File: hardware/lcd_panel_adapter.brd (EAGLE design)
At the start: 54 x 30 mm, 50 parts, among them IC1 TPS65131RGET, IC2 LP8867CQPWPRQ1, J1 245863050104829+, J2 54548-2271, U1 TLV62080DSGR

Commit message: added +1.8V pullup resistor for LCD reset pin
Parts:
- added R16: 10k, rcl:R0603
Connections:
- net 1V8: now also R16.2
- net LCD_RESET_N: now also R16.1
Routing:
- net LCD_RESET_N: track 24.2 -> 43.9 mm
- net 1V8: track 33.3 -> 35.9 mm
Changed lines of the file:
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@@
 </element>
 <element name="R7" library="rcl" library_urn="urn:adsk.eagle:library:334" package="R0603" package3d_urn="urn:adsk.eagle:package:23555/3" value="150k" x="12" y="22.5" smashed="yes" rot="R90">
-<attribute name="NAME" x="12.745" y="25.925" size="0.8128" layer="25" rot="R180"/>
+<attribute name="NAME" x="14.095" y="24.875" size="0.8128" layer="25" rot="R180"/>
 <attribute name="POPULARITY" value="70" x="12" y="22.5" size="1.778" layer="27" rot="R90" display="off"/>
 <attribute name="SPICEPREFIX" value="R" x="12" y="22.5" size="1.778" layer="27" rot="R90" display="off"/>
@@
 <attribute name="SPICEPREFIX" value="C" x="35.71" y="26.09" size="1.778" layer="27" rot="R90" display="off"/>
 <attribute name="VALUE" x="38.25" y="24.82" size="1.27" layer="27" rot="R90"/>
+</element>
+<element name="R16" library="rcl" library_urn="urn:adsk.eagle:library:334" package="R0603" package3d_urn="urn:adsk.eagle:package:23555/3" value="10k" x="12.55" y="26.6" smashed="yes" rot="R270">
+<attribute name="NAME" x="11.165" y="25.615" size="0.8128" layer="25" rot="R90"/>
+<attribute name="POPULARITY" value="70" x="12.55" y="26.6" size="1.778" layer="27" rot="R270" display="off"/>
+<attribute name="SPICEPREFIX" value="R" x="12.55" y="26.6" size="1.778" layer="27" rot="R270" display="off"/>
+<attribute name="VALUE" x="10.645" y="27.235" size="1.27" layer="27" rot="R270"/>
 </element>
 </elements>
@@
 <wire x1="26.94" y1="23.96" x2="27.596" y2="24.616" width="0.127" layer="1"/>
 <wire x1="27.596" y1="24.616" x2="27.6" y2="24.616" width="0.127" layer="1"/>
+<wire x1="45.648" y1="17.375" x2="51.51" y2="19.41" width="0" layer="19" extent="1-1"/>
+<wire x1="42.71" y1="15.39" x2="42.71" y2="16.4" width="0" layer="19" extent="1-1"/>
+<wire x1="45.648" y1="14.775" x2="45.648" y2="17.375" width="0" layer="19" extent="1-1"/>
+<wire x1="39.772" y1="14.125" x2="42.66" y2="15.34" width="0" layer="19" extent="1-1"/>
+<wire x1="39.8" y1="10.55" x2="38.33" y2="13.62" width="0" layer="19" extent="1-1"/>
+<wire x1="35.14" y1="16.83" x2="38.33" y2="13.62" width="0" layer="19" extent="1-1"/>
+<wire x1="35" y1="19" x2="35.14" y2="16.83" width="0" layer="19" extent="1-1"/>
+<wire x1="35.29" y1="22.44" x2="35" y2="19" width="0" layer="19" extent="1-1"/>
+<wire x1="37.39" y1="22.45" x2="35.3" y2="22.45" width="0" layer="19" extent="1-1"/>
+<wire x1="39.5" y1="22.45" x2="37.4" y2="22.45" width="0" layer="19" extent="1-1"/>
+<wire x1="32.21" y1="25.395" x2="35.3" y2="22.45" width="0" layer="19" extent="1-1"/>
+<wire x1="35.7" y1="27.5" x2="35.71" y2="27.49" width="0" layer="19" extent="1-1"/>
+<wire x1="38.7" y1="27.5" x2="38.68" y2="27.48" width="0" layer="19" extent="1-1"/>
+<wire x1="16.57" y1="23.81" x2="18.74" y2="23.83" width="0" layer="19" extent="1-1"/>
+<wire x1="12" y1="23.35" x2="15.02" y2="23.81" width="0" layer="19" extent="1-1"/>
+<wire x1="9.86" y1="23.39" x2="12" y2="23.35" width="0" layer="19" extent="1-1"/>
+<wire x1="9.53" y1="18.9" x2="9.86" y2="22.15" width="0" layer="19" extent="1-1"/>
+<wire x1="8.28" y1="16.95" x2="9" y2="17.7" width="0" layer="19" extent="1-1"/>
+<wire x1="6.33" y1="17.7" x2="6.33" y2="17.2" width="0" layer="19" extent="1-1"/>
+<wire x1="9" y1="16.2" x2="8.28" y2="16.95" width="0" layer="19" extent="1-1"/>
+<wire x1="15.19" y1="27.47" x2="15.02" y2="23.81" width="0" layer="19" extent="1-1"/>
+<wire x1="17.26" y1="28.7" x2="15.19" y2="28.68" width="0" layer="19" extent="1-1"/>
+<wire x1="13.25" y1="19.9" x2="12" y2="23.35" width="0" layer="19" extent="1-1"/>
+<wire x1="14.1" y1="18.15" x2="14.52" y2="19.9" width="0" layer="19" extent="1-1"/>
+<wire x1="17.97" y1="18.8" x2="15.54" y2="18.15" width="0" layer="19" extent="1-1"/>
+<wire x1="20.13" y1="18.76" x2="17.97" y2="18.8" width="0" layer="19" extent="1-1"/>
+<wire x1="2.3" y1="15.15" x2="6.33" y2="17.2" width="0" layer="19" extent="1-1"/>
+<wire x1="2.75" y1="13.4" x2="2.3" y2="15.15" width="0" layer="19" extent="1-1"/>
+<wire x1="4.62" y1="11.12" x2="2.75" y2="13.4" width="0" layer="19" extent="1-1"/>
+<wire x1="8.6" y1="8.55" x2="6.63" y2="11.14" width="0" layer="19" extent="1-1"/>
+<wire x1="5.84" y1="7.94" x2="8.6" y2="8.55" width="0" layer="19" extent="1-1"/>
+<wire x1="7.63" y1="5.19" x2="5.8" y2="6.75" width="0" layer="19" extent="1-1"/>
+<wire x1="25.42" y1="13.06" x2="20.13" y2="17.3" width="0" layer="19" extent="1-1"/>
+<wire x1="25.54" y1="10.43" x2="25.42" y2="13.06" width="0" layer="19" extent="1-1"/>
+<wire x1="26.56" y1="8.81" x2="25.54" y2="10.43" width="0" layer="19" extent="1-1"/>
+<wire x1="26.89" y1="6.33" x2="26.56" y2="8.81" width="0" layer="19" extent="1-1"/>
+<wire x1="25.39" y1="6.33" x2="26.89" y2="6.33" width="0" layer="19" extent="1-1"/>
+<wire x1="22.39" y1="6.33" x2="23.89" y2="6.33" width="0" layer="19" extent="1-1"/>
+<wire x1="17.12" y1="4.43" x2="17.115" y2="4.43" width="0" layer="19" extent="1-1"/>
+<wire x1="32.16" y1="4.43" x2="28.39" y2="6.33" width="0" layer="19" extent="1-1"/>
 </signal>
 <signal name="+5V">
@@
 <wire x1="15.06" y1="11.06" x2="16.3722" y2="12.3722" width="0.4" layer="15"/>
 <wire x1="13.82" y1="22.85" x2="13.82" y2="24.7" width="0.4" layer="15"/>
-<wire x1="13.82" y1="24.7" x2="14.89" y2="25.77" width="0.4" layer="15"/>
+<wire x1="13.82" y1="24.7" x2="14.06" y2="24.94" width="0.4" layer="15"/>
+<wire x1="14.06" y1="24.94" x2="14.89" y2="25.77" width="0.4" layer="15"/>
 <wire x1="14.89" y1="25.77" x2="15.19" y2="25.77" width="0.4" layer="15"/>
 <via x="15.19" y="25.77" extent="1-16" drill="0.35"/>
 <wire x1="13.51" y1="9.51" x2="15.06" y2="11.06" width="0.4" layer="1"/>
 <wire x1="16.3722" y1="20.2978" x2="13.82" y2="22.85" width="0.4" layer="15"/>
+<contactref element="R16" pad="2"/>
+<wire x1="12.55" y1="25.75" x2="12.58" y2="25.78" width="0.4" layer="1"/>
+<wire x1="12.58" y1="25.78" x2="15.2" y2="25.78" width="0.4" layer="1"/>
 </signal>
 <signal name="FB">
@@
 <wire x1="48.9" y1="29.64" x2="51.51" y2="27.03" width="0.127" layer="1"/>
 <wire x1="31.04" y1="29.64" x2="48.9" y2="29.64" width="0.127" layer="1"/>
+<contactref element="R16" pad="1"/>
+<wire x1="12.55" y1="27.45" x2="12.55" y2="27.95" width="0.127" layer="1"/>
+<wire x1="14.24" y1="29.64" x2="31.04" y2="29.64" width="0.127" layer="1"/>
+<wire x1="12.55" y1="27.95" x2="14.24" y2="29.64" width="0.127" layer="1"/>
 </signal>
 <signal name="LCD_BL_LEDPWM">

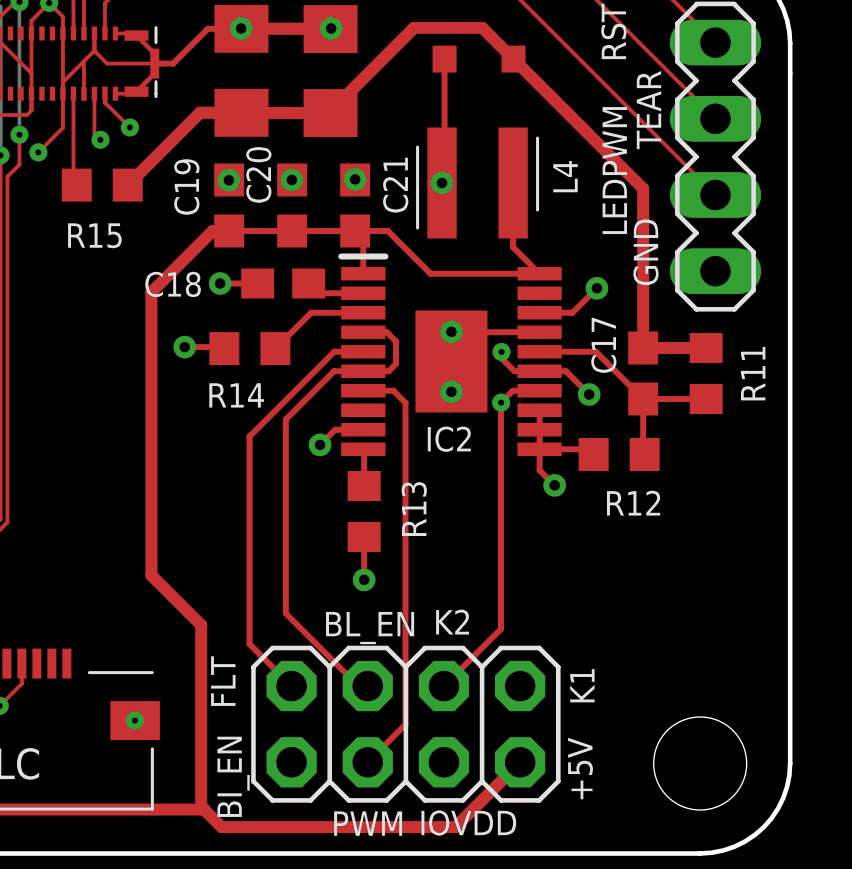
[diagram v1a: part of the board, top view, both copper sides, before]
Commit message: updated the backlight driver IC from LP8867 to TPS61194
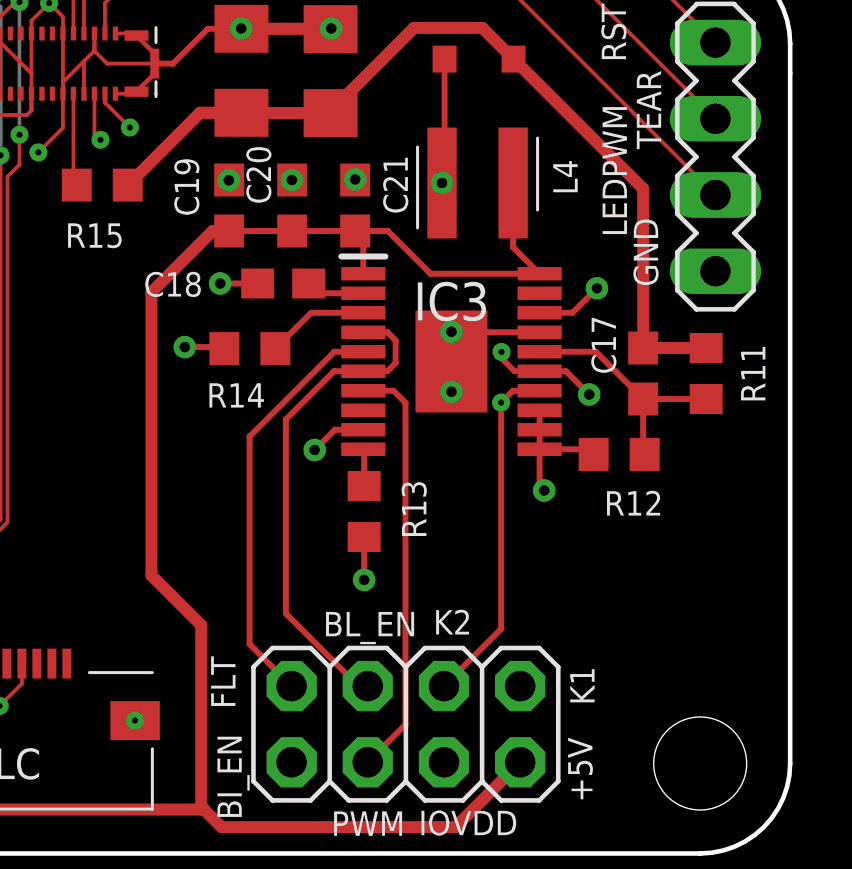
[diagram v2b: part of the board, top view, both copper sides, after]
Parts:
- C12: value 12pF -> 75pF
- C8: value 15pF -> 12pF
- IC3: value LP8867CQPWPRQ1 -> TPS61194PWPR
- R13: value 60k -> 62k
- renumbered IC2 to IC3
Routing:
- net LCD_BL_K2: track 30.8 -> 29.3 mm
- net GND: track 114.5 -> 115.0 mm

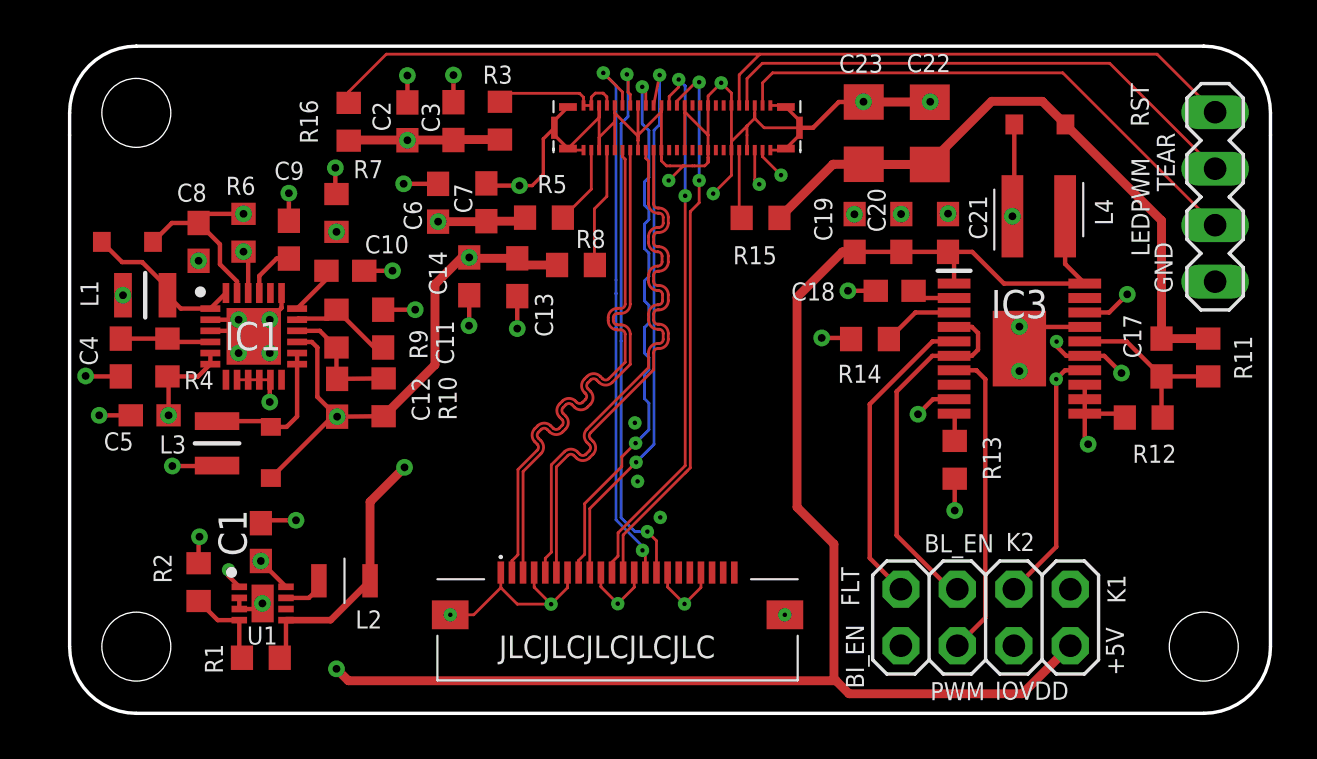
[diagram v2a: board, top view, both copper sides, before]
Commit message: revert back from TPS61194 to LP8867, and add transistors
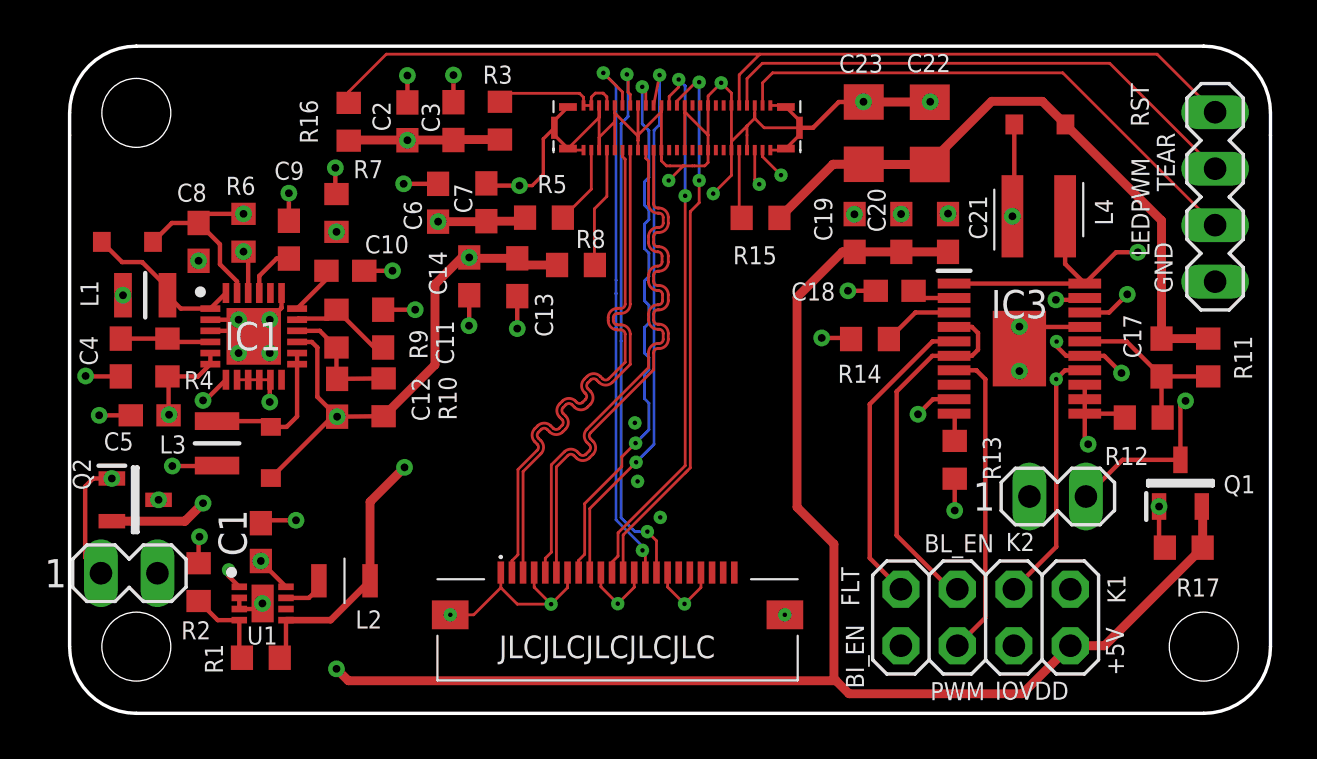
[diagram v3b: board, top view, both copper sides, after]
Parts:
- added Q1, Q2: SI2319DDS-T1-GE3, SamacSys_Parts:SOT96P240X120-3N
- added R17: 20k, rcl:R0603
- added U$5, U$6: MA02-1, custom_library:MA02-1
- IC3: value TPS61194PWPR -> LP8867CQPWPRQ1
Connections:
- new net BIAS_DRAIN: L1.1, Q2.3, U$5.2
- new net BIAS_GATE: IC1.7, Q2.1, U$5.1
- new net BL_DRAIN: IC3.1, IC3.20, L4.1, Q1.3, U$6.2
- new net BL_GATE: IC3.19, Q1.1, R17.2, U$6.1
- net +5V: now also Q1.2, Q2.2, R17.1; no longer IC3.1, IC3.20, L1.1, L4.1
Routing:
- net BL_DRAIN: track 0.00 -> 27.5 mm, vias 0 -> 2
- net BL_GATE: track 0.00 -> 22.1 mm, vias 0 -> 2
- net BIAS_DRAIN: track 0.00 -> 13.2 mm, vias 0 -> 2
- net BIAS_GATE: track 0.00 -> 12.8 mm, vias 0 -> 2
- net +5V: track 99.2 -> 95.8 mm
